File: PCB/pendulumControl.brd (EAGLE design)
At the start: 47.9 x 33.9 mm, 29 parts, among them IC1 PIC32MX340F512H, IC2 LT1963EST-3.3

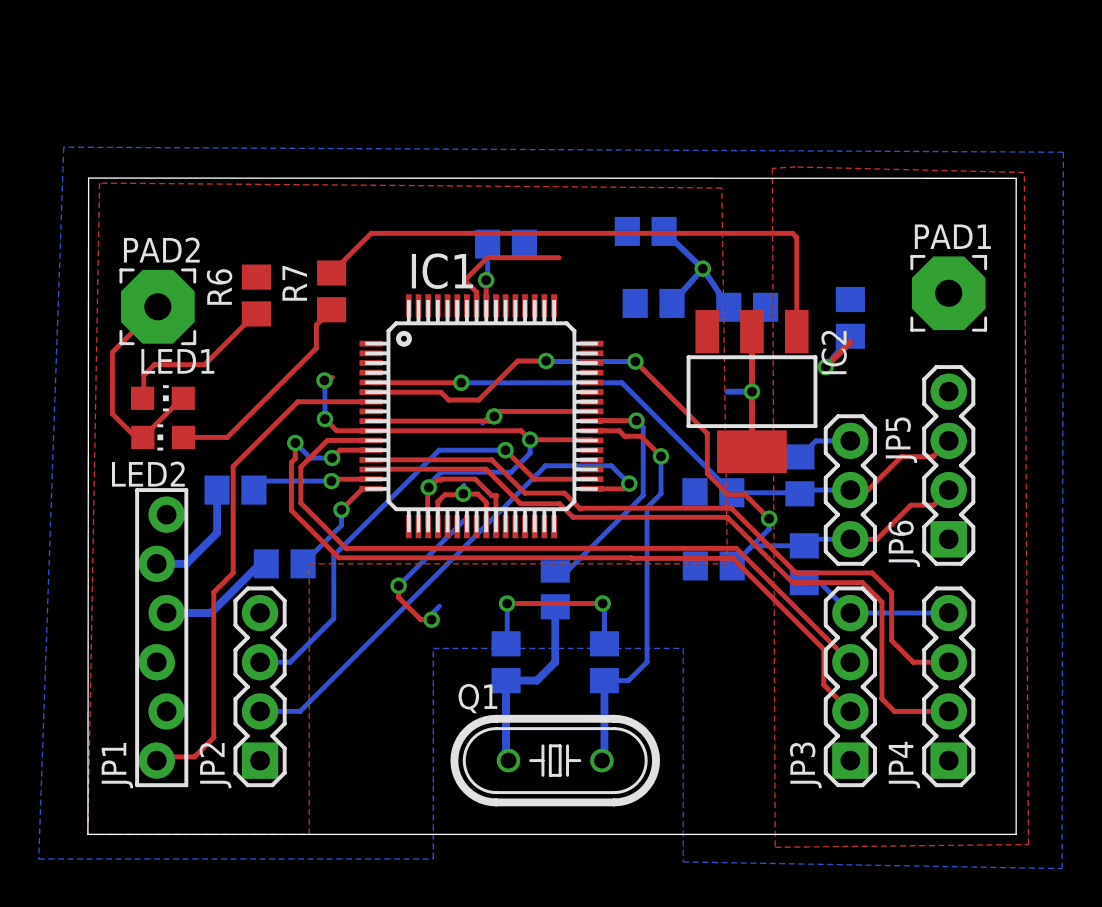
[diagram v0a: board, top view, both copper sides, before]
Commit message: Added Mounting Holes. Updated the setup.
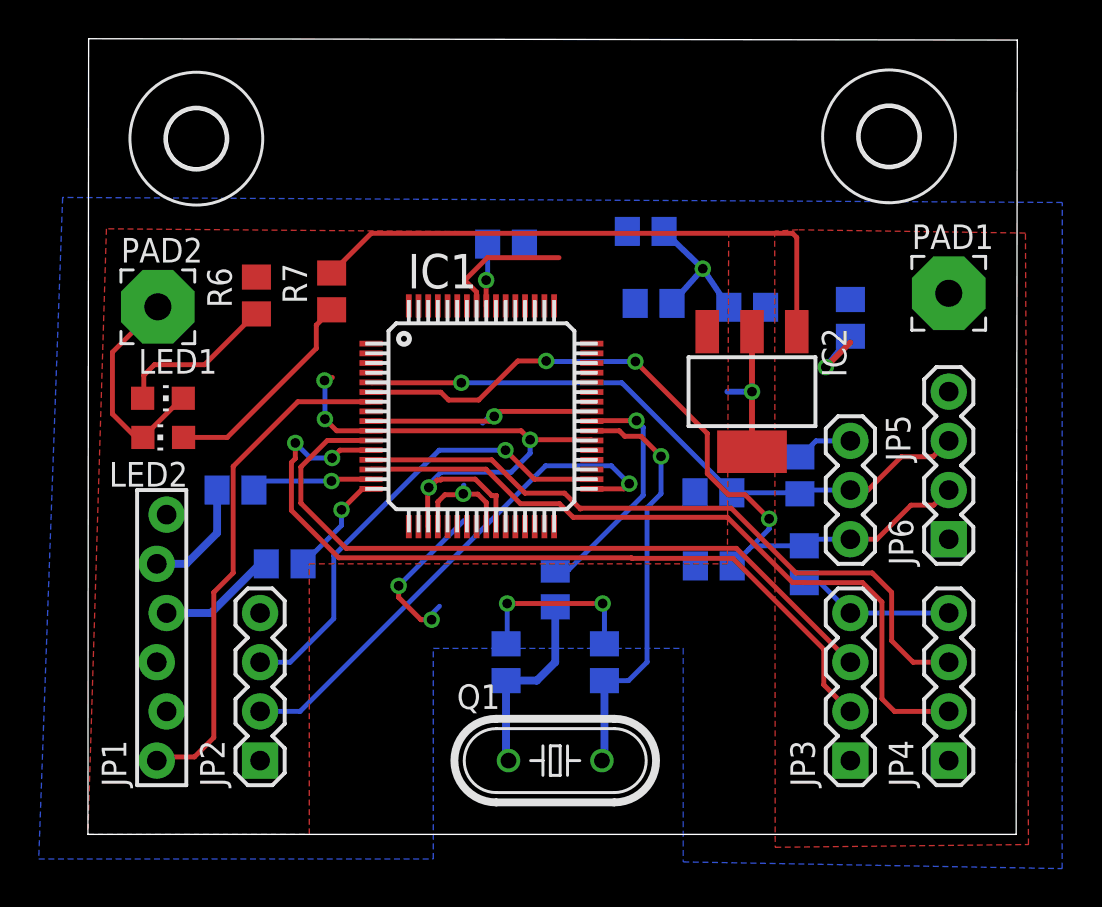
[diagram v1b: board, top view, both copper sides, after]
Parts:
- added U$1, U$2: (no value), holes:3,0
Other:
- board size 47.9 x 33.9 mm -> 48 x 41.1 mm
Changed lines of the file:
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@@
 <?xml version="1.0" encoding="utf-8"?>
 <!DOCTYPE eagle SYSTEM "eagle.dtd">
-<eagle version="7.2.0">
+<eagle version="7.3.0">
 <drawing>
 <settings>
@@
 <plain>
 <wire x1="0" y1="0" x2="47.93" y2="0" width="0" layer="20"/>
-<wire x1="47.93" y1="0" x2="47.9322125" y2="33.87758125" width="0" layer="20"/>
-<wire x1="47.9322125" y1="33.87758125" x2="0.035809375" y2="33.88759375" width="0" layer="20"/>
-<wire x1="0.035809375" y1="33.88759375" x2="0" y2="0" width="0" layer="20"/>
-<dimension x1="0.035809375" y1="33.88759375" x2="0" y2="0" x3="-1.4867375" y3="16.9453875" textsize="1.778" layer="20" unit="inch"/>
-<dimension x1="0.035809375" y1="33.88759375" x2="47.9322125" y2="33.87758125" x3="23.984290625" y3="35.229678125" textsize="1.778" layer="20" unit="inch"/>
-<dimension x1="0.035809375" y1="33.88759375" x2="47.9322125" y2="33.87758125" x3="23.984859375" y3="37.95588125" textsize="1.778" layer="20"/>
-<dimension x1="0.035809375" y1="33.88759375" x2="0" y2="0" x3="-4.2101125" y3="16.948265625" textsize="1.778" layer="20"/>
+<wire x1="47.93" y1="0" x2="47.991140625" y2="41.015465625" width="0" layer="20"/>
+<wire x1="47.991140625" y1="41.015465625" x2="0.035809375" y2="41.08446875" width="0" layer="20"/>
+<wire x1="0.035809375" y1="41.08446875" x2="0" y2="0" width="0" layer="20"/>
 </plain>
 <attributes>
@@
 <element name="PAD1" library="wirepad" package="3,81/1,4" value="" x="44.45" y="27.94"/>
 <element name="PAD2" library="wirepad" package="3,81/1,4" value="" x="3.610971875" y="27.242328125"/>
+<element name="U$1" library="holes" package="3,0" value="" x="5.59806875" y="35.925396875"/>
+<element name="U$2" library="holes" package="3,0" value="" x="41.366775" y="36.043378125"/>
 </elements>
 <signals>
@@
 <contactref element="IC2" pad="2"/>
 <polygon width="0.4064" layer="16">
-<vertex x="-1.246740625" y="35.4843625"/>
+<vertex x="-1.30566875" y="32.88876875"/>
 <vertex x="-2.54" y="-1.27"/>
 <vertex x="17.835128125" y="-1.27"/>
@@
 <vertex x="30.738575" y="-1.420375"/>
 <vertex x="50.3033875" y="-1.767528125"/>
-<vertex x="50.3689125" y="35.2251"/>
+<vertex x="50.309984375" y="32.62950625"/>
 </polygon>
 <contactref element="PAD2" pad="1"/>
@@
 <vertex x="11.43" y="13.97"/>
 <vertex x="33.02" y="13.97"/>
-<vertex x="32.733365625" y="33.37505"/>
-<vertex x="0.601965625" y="33.629290625"/>
+<vertex x="33.086928125" y="31.01541875"/>
+<vertex x="0.955528125" y="31.269659375"/>
 </polygon>
 <wire x1="33.09125" y1="27.21803125" x2="31.75" y2="29.21" width="0.3048" layer="16"/>
@@
 <contactref element="PAD1" pad="1"/>
 <polygon width="0.4064" layer="1">
-<vertex x="36.543365625" y="34.463128125"/>
-<vertex x="35.34505" y="34.391353125"/>
+<vertex x="36.66121875" y="31.218634375"/>
+<vertex x="35.462903125" y="31.146859375"/>
 <vertex x="35.48835" y="-0.666996875"/>
 <vertex x="48.566303125" y="-0.523484375"/>
-<vertex x="48.35131875" y="34.176196875"/>
+<vertex x="48.41024375" y="31.049684375"/>
 </polygon>
 <wire x1="39.37" y1="25.72" x2="38.1" y2="24.13" width="0.3048" layer="16"/>
